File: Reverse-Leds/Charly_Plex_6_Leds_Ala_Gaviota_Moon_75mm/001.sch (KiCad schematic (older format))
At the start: 11 parts, among them J1 Conn_01x02, J2 Conn_01x06_x03, U1 PCB, U2 Firma

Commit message: UpdateMoon
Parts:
- added U3: Oshpark_logo, Reverse_Mount_Leds:OSHpark-1-1200, symbol 001-rescue:PCB-Reverse_mount_leds
- added U4: Oshpark_Purple, Reverse_Mount_Leds:OSHpark-2-1800, symbol 001-rescue:PCB-Reverse_mount_leds
- added U5: OSHW_Silk, Symbol:OSHW-Logo2_9.8x8mm_SilkScreen, symbol 001-rescue:PCB-Reverse_mount_leds
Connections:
- net VCC: now also BT1.1 (+), J1.1 (Pin_1)
- net VIN: no longer BT1.1 (+), J1.1 (Pin_1)
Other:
- note added: "Coin Battery"
- note added: "DigiSpark"
- note added: "Flags"
- note added: "Lipo Battery"
- moved on the sheet: BT1, D1, D2, D3, D4, D5, D6, J1, U1, U2

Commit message: Changes Moon
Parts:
- J2: symbol Digispark:Conn_01x06_x03 -> 001-rescue:Conn_01x06_x03-Digispark
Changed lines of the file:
@@
 $EndComp
 $Comp
-L Digispark:Conn_01x06_x03 J2
+L 001-rescue:Conn_01x06_x03-Digispark J2
 U 1 1 5DA5B104
 P 1825 1900

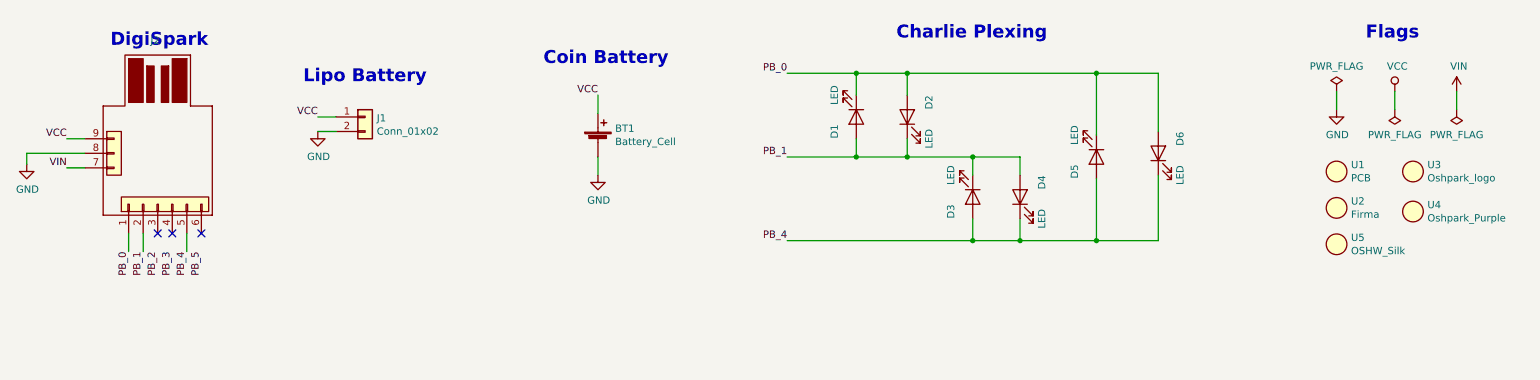
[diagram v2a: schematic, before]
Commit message: Add Attiny85 Breakout
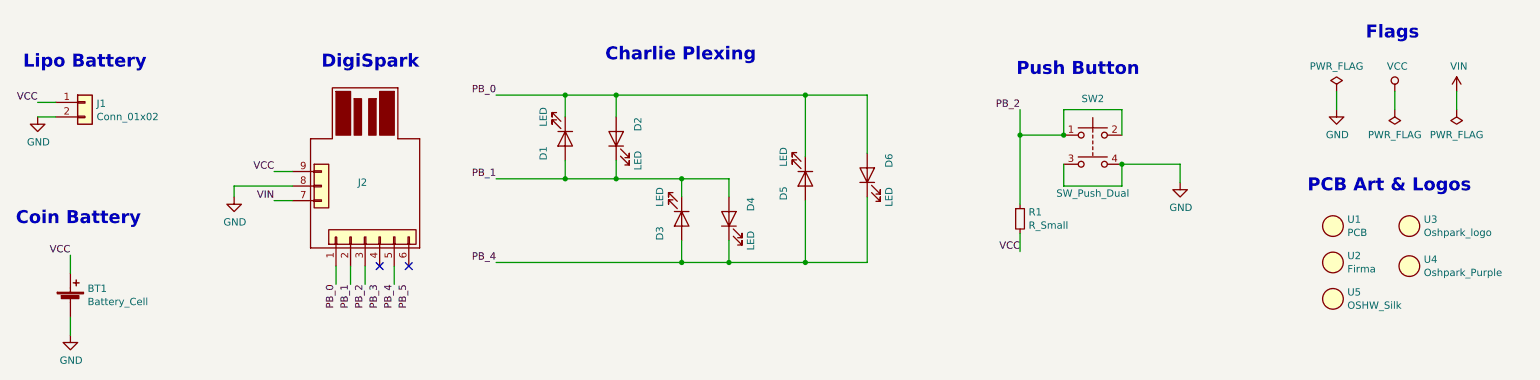
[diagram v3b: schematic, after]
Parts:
- added R1: R_Small, Resistor_SMD:R_1206_3216Metric_Pad1.42x1.75mm_HandSolder, symbol Device:R_Small
- added SW2: SW_Push_Dual, Moon_75mm_Gaviota:SW_Push_PTS647_4.5mm, symbol Switch:SW_Push_Dual
- BT1: footprint Battery:S8211R -> Moon_75mm_Gaviota:S8211R
- D1, D2, D3, D4, D5, D6: footprint Reverse_Mount_Leds:SunLed_PLCC_Reverse-2 -> Moon_75mm_Gaviota:SunLed_PLCC_Reverse-2
- J1: footprint Connector_JST:JST-S2B-PH-SM4-TB -> Moon_75mm_Gaviota:JST-S2B-PH-SM4-TB
- J2: footprint Reverse_Mount_Leds:Digispark_SMD_Reverse -> Moon_75mm_Gaviota:Digispark_SMD_Reverse
- U1: footprint Reverse_Mount_Leds:Moon_6_Leds_75_2 -> Moon_75mm_Gaviota:Moon_6_Leds_75_2
- U2: footprint Reverse_Mount_Leds:firma_Cu_Mask -> Moon_75mm_Gaviota:firma_Cu_Mask
- U3: footprint Reverse_Mount_Leds:OSHpark-1-1200 -> Moon_75mm_Gaviota:OSHpark-1-1200
- U4: footprint Reverse_Mount_Leds:OSHpark-2-1800 -> Moon_75mm_Gaviota:OSHpark-2-1800
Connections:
- net GND: now also SW2.3, SW2.4
- net PB_2: now also J2.3 (P2_D2), R1.1, SW2.1, SW2.2
- net VCC: now also R1.2
- no-connect marks 3 -> 2
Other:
- note added: "PCB Art & Logos"
- note added: "Push Button"
- moved on the sheet: BT1, D1, D2, D3, D4, D5, D6, J1, J2, U1, U2, U3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
